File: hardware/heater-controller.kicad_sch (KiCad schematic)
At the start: 9 parts, among them J1 Vitotronic plug 96, Q1 SFH 309 FA

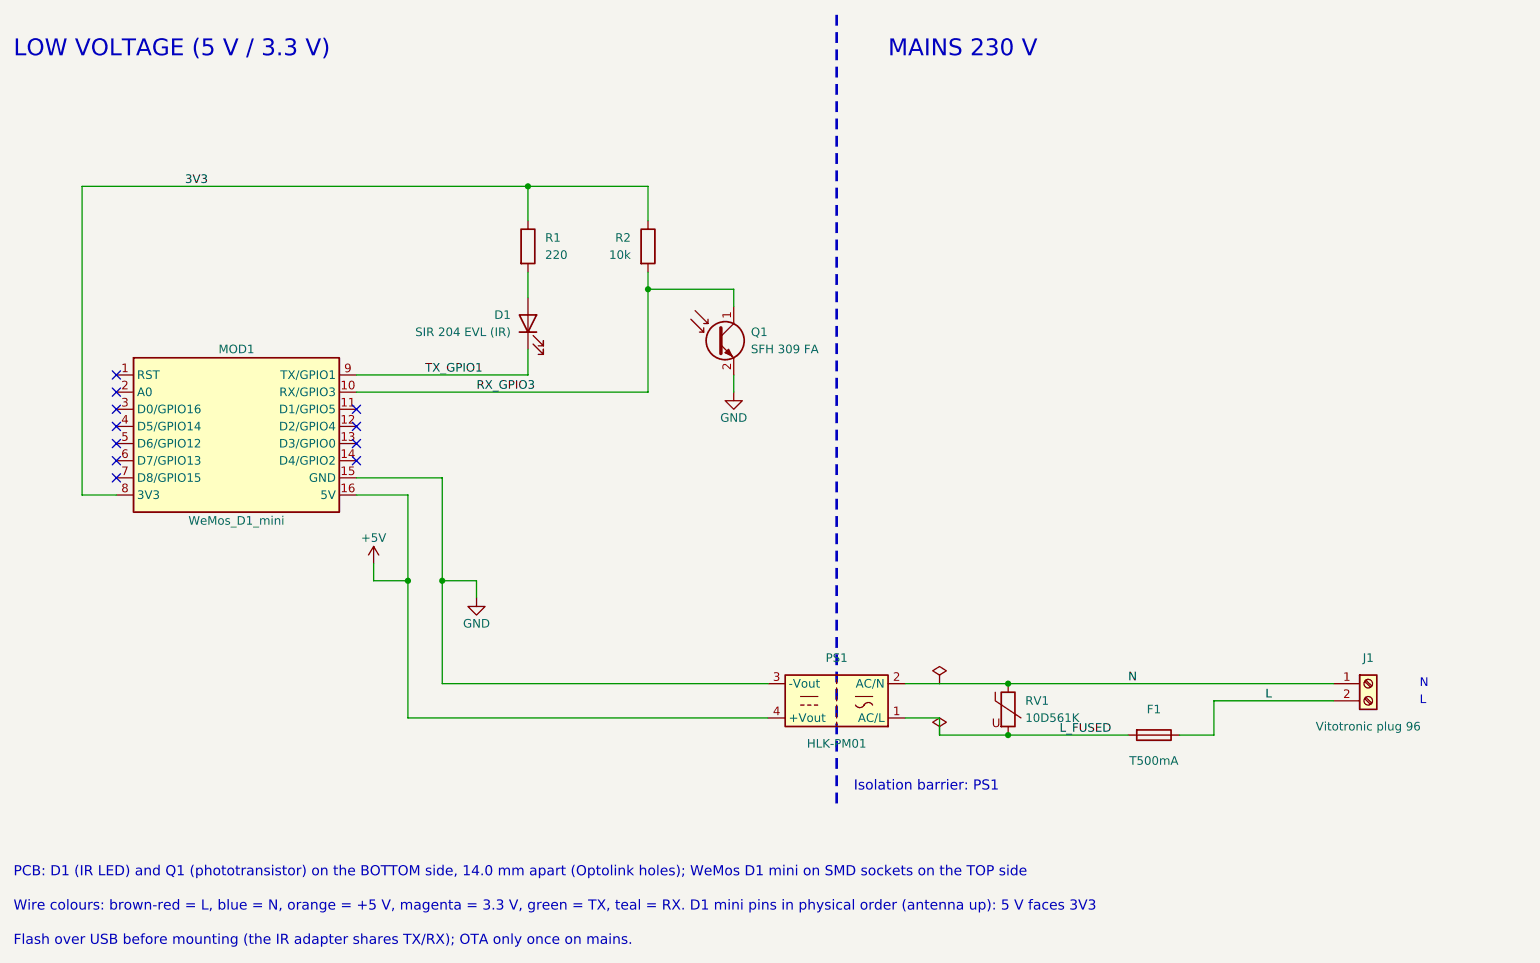
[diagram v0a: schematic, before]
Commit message: feat(hardware): move to ESP32-C3 on a removable U-shaped board (#1)
* feat(hardware): move to ESP32-C3 on a removable U-shaped board

- ESP32-C3 super mini replaces the D1 mini: Optolink UART on GPIO4/GPIO3,
  logs over native USB
- inverted U board (86 x 39.5 mm): 230 V leg, optical head header on the bar,
  C3 on SMD female sockets; screw terminal for the mains wires
- off-board optical head on a 4-wire ribbon
- back GND pour, 0.7 mm power tracks, 6 mm mains isolation checked by DRC
- C3 socket footprint generator and fabrication export script
- enclosure redrawn around the new board

* feat(hardware): hand-solderable board with SMD C3 sockets for JLCPCB

- C3 plugged into two hanxia 1x8 SMD sockets (J3/J4) at 15.24 mm, the only
  parts with an LCSC number; MOD1 off board with a board-only outline
- through-hole everything else: TR5 T1A fuse, 07D431K varistor, JST PH
  vertical optical head connector, axial resistors
- HLK-PM01 footprint from the Hi-Link datasheet (15.4 / 29.4 mm pin pitch)
- footprints generated by footprints.py from the datasheets
- export adds the JLCPCB BOM and placement files
- routing done in KiCad: 0.7 mm power tracks, no ground plane

* feat(hardware): source every part at LCSC with datasheet footprints

- Kefa KF128 terminal block (Phoenix MKDS out of stock), Bourns MOV-07D431K
  inline varistor and JST PH with 0.9 mm holes, drawn by footprints.py
- LCSC number on every part; split-bom.py writes the JLCPCB BOM (SMD only)
  and an LCSC cart for the hand-soldered parts
- RV1 rerouted for its inline leads; DRC clean, schematic parity
- Enclosure split into named bodies: shells, lid, optical plug
- READMEs: parts list with suppliers, prices and footprint specs
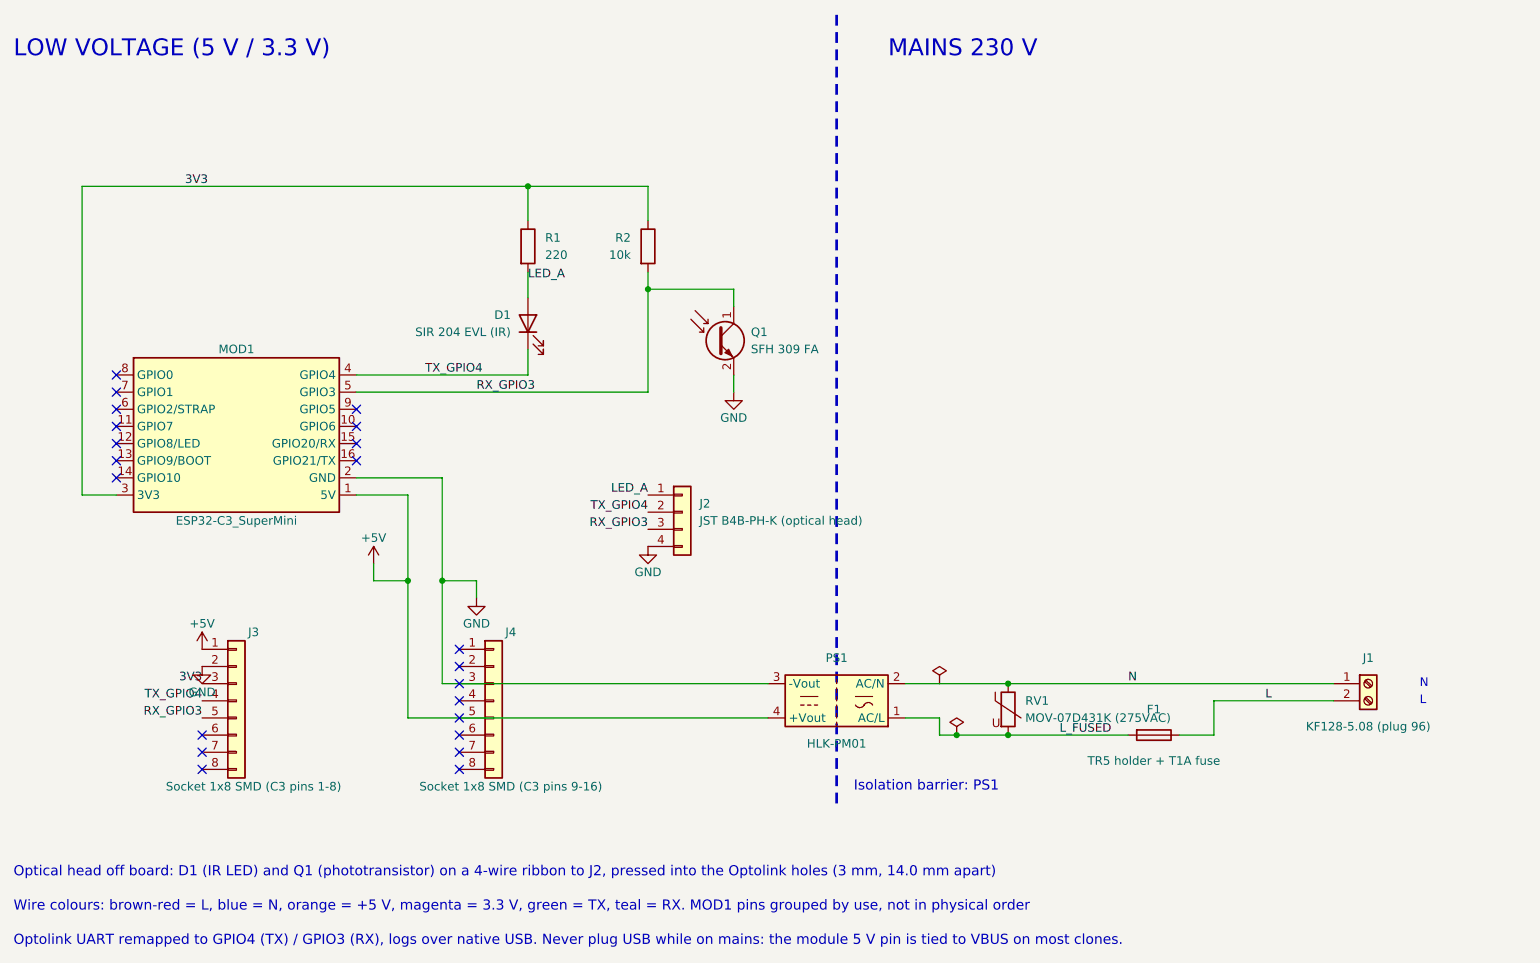
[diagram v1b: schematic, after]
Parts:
- added J2: JST B4B-PH-K (optical head), heater-controller:JST_PH_B4B-PH-K_1x04_P2.00mm_Vertical_Drill0.9, symbol Connector_Generic:Conn_01x04
- added J3: Socket 1x8 SMD (C3 pins 1-8), heater-controller:PinSocket_1x08_P2.54mm_SMD_HX-ZQ, symbol Connector_Generic:Conn_01x08
- added J4: Socket 1x8 SMD (C3 pins 9-16), heater-controller:PinSocket_1x08_P2.54mm_SMD_HX-ZQ, symbol Connector_Generic:Conn_01x08
- D1, Q1: now left out of the parts list
- F1: value T500mA -> TR5 holder + T1A fuse; footprint Fuse:Fuseholder_Cylinder-5x20mm_Bulgin_FX0456_Vertical_Closed -> Fuse:Fuseholder_TR5_Littelfuse_No560_No460; LCSC (none) -> C142909
- J1: value Vitotronic plug 96 -> KF128-5.08 (plug 96); footprint TerminalBlock_Phoenix:TerminalBlock_Phoenix_MKDS-1,5-2-5.08_1x02_P5.08mm_Horizontal -> heater-controller:TerminalBlock_Kefa_KF128-5.08_1x02; LCSC (none) -> C474952
- MOD1: value WeMos_D1_mini -> ESP32-C3_SuperMini; footprint heater-controller:WEMOS_D1_mini_SMD_sockets -> (none); symbol heater-controller:WeMos_D1_mini -> heater-controller:ESP32-C3_SuperMini; now left out of the parts list
- PS1: footprint Converter_ACDC:Converter_ACDC_Hi-Link_HLK-PMxx -> heater-controller:Converter_ACDC_HLK-PM01; LCSC (none) -> C209903
- R1, R2: footprint Resistor_SMD:R_0805_2012Metric -> Resistor_THT:R_Axial_DIN0207_L6.3mm_D2.5mm_P7.62mm_Horizontal
- RV1: value 10D561K -> MOV-07D431K (275VAC); footprint Varistor:RV_Disc_D12mm_W4.2mm_P7.5mm -> heater-controller:RV_Disc_D9mm_W4.8mm_P5mm_Inline; LCSC (none) -> C1528105
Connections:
- net +5V: now also MOD1.1 (5V), J3.1 (Pin_1); no longer MOD1.16 (5V)
- net 3V3: now also MOD1.3 (3V3), J3.3 (Pin_3); no longer MOD1.8 (3V3)
- net GND: now also MOD1.2 (GND), J2.4 (Pin_4), J3.2 (Pin_2); no longer MOD1.15 (GND)
- net RX_GPIO3: now also MOD1.5 (GPIO3), J2.3 (Pin_3), J3.5 (Pin_5); no longer MOD1.10 (RX/GPIO3)
- net TX_GPIO4: now reaches MOD1.4 (GPIO4)
- net TX_GPIO4: now also D1.1 (K), J2.2 (Pin_2), J3.4 (Pin_4)
- net LED_A: now reaches D1.2 (A), R1.2
- net LED_A: now also J2.1 (Pin_1)
- net TX_GPIO1: no longer names the net of MOD1.9 (GPIO5)
- net TX_GPIO1: no longer D1.1 (K)
- no-connect marks 11 -> 22
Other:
- note added: "Optical head off board: D1 (IR LED) and Q1 (phototransistor) on a 4-wire ribbon to J2, pressed into the Optolink holes (3 mm, 14.0 mm apart)"
- note added: "Optolink UART remapped to GPIO4 (TX) / GPIO3 (RX), logs over native USB. Never plug USB while on mains: the module 5 V pin is tied to VBUS on most clones."
- note added: "Wire colours: brown-red = L, blue = N, orange = +5 V, magenta = 3.3 V, green = TX, teal = RX. MOD1 pins grouped by use, not in physical order"
- note removed: "Flash over USB before mounting (the IR adapter shares TX/RX); OTA only once on mains."
- note removed: "PCB: D1 (IR LED) and Q1 (phototransistor) on the BOTTOM side, 14.0 mm apart (Optolink holes); WeMos D1 mini on SMD sockets on the TOP side"
- note removed: "Wire colours: brown-red = L, blue = N, orange = +5 V, magenta = 3.3 V, green = TX, teal = RX. D1 mini pins in physical order (antenna up): 5 V faces 3V3"
